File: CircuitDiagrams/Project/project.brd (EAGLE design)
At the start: 100 x 70 mm, 55 parts, among them IC1 UC3C, IC2 PCA9542A, IC3 MT48LC4M16A2TSOP54, IC4 TB6593FNGSSOP20, IC5 TB6593FNGSSOP20, J2 1BY2THROUGHHOLE, J3 1BY2THROUGHHOLE, Q1 OV7670, Q2 OV7670, Q3 VREGSOT-223, Q4 TCRT1010TH, Q5 TCRT1010TH, X2 MICROSDSMD

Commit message: Done some more on PCB, mainly adding decoupling capacitors (lots of)
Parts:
- added C10, C8: 4.7u, passives:C1206
- added C11, C13, C15, C17, C20: 33n, passives:C1206
- added C12, C14, C16, C19, C21, C7: 100n, passives:C1206
- added C18, C24, C27, C29, C32, C33, C42: 100n, passives:C0603
- added C22, C25, C28, C30, C43, C9: 33n, passives:C0603
- added C23, C26: 4.7u, passives:C0603
- added C34, C36, C38, C39: 0.1u, passives:C0603
- added C35, C37, C40, C41: 10u, passives:SMC_Z
- added C5: 2.2u, passives:C1206
- added C6: 1n, passives:C1206
- added Q6: CSM-7X-DU, crystal:CSM-7X-DU
- added R36: 1k5, passives:R0603
- moved C1 39.8 mm to (55.7, 31.4)
- moved C2 19.4 mm to (56.7, 51.8)
- moved S1 12.2 mm to (47.5, 50.3)
- moved R1 10.4 mm to (46.9, 55.1)
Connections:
- new net ADCREFN: C21.2, C22.2, IC1.35
- new net ADCREFP: C21.1, C22.1, IC1.34
- new net N$32: R36.1, X2.CD
- net +3V3: now also C10.1, C11.1, C12.1, C13.1, C14.1, C15.1, C16.1, C17.1, C18.1, C19.1, C20.1, C23.1, C24.1, C25.1, C26.1, C27.1, C28.1, C29.1, C30.1, C32.1, C33.1, C34.1, C35.+, C36.1, C37.+, C38.1, C39.1, C40.+, C41.+, C42.1, C43.1, C5.1, C6.1, C7.1, C8.1, C9.1
- net GND: now also C1.2, C10.2, C11.2, C12.2, C13.2, C14.2, C15.2, C16.2, C17.2, C18.2, C19.2, C2.2, C20.2, C23.2, C24.2, C25.2, C26.2, C27.2, C28.2, C29.2, C30.2, C32.2, C33.2, C34.2, C35.-, C36.2, C37.-, C38.2, C39.2, C40.-, C41.-, C42.2, C43.2, C5.2, C6.2, C7.2, C8.2, C9.2, X2.SW
- net PB0: now also C2.1, Q6.1
- net PB1: now also C1.1, Q6.2

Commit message: Placed all components. Need to confirm the circuit diagram and complete that before routing
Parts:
- C1, C10, C11, C12, C13, C14, C15, C16, C17, C19, C2, C20, C21, C5, C6, C7, C8: device passives:C1206 -> passives:C0603
- C3, C4: device passives:SMC_E -> passives:SMC_P
- moved R36 335.6 mm to (18.0, 62.0), turned to 270 degrees
- moved C43 333.4 mm to (98.0, 30.0), turned to 90 degrees
- moved C42 322.6 mm to (94.0, 30.0), turned to 90 degrees
- moved C35 296.5 mm to (16.0, 45.0), flipped to the bottom
- moved C38 296.5 mm to (15.0, 29.0), flipped to the bottom
- moved C37 294.6 mm to (16.0, 39.0), flipped to the bottom
- moved C39 293.2 mm to (15.0, 26.0), flipped to the bottom
- moved C36 289.6 mm to (16.0, 42.0), flipped to the bottom
- moved C34 287.6 mm to (16.0, 48.0), flipped to the bottom
- moved C40 284.5 mm to (15.0, 23.0), flipped to the bottom
- moved C41 281.3 mm to (15.0, 20.0), flipped to the bottom
- moved C32 281.0 mm to (3.00, 51.0), turned to 180 degrees
- moved C30 278.6 mm to (98.0, 39.0), turned to 90 degrees
- moved C29 273.4 mm to (94.0, 39.0), turned to 90 degrees
- moved C33 266.6 mm to (79.0, 20.0), flipped to the bottom, turned to 270 degrees
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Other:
- outline, holes or cut-outs redrawn

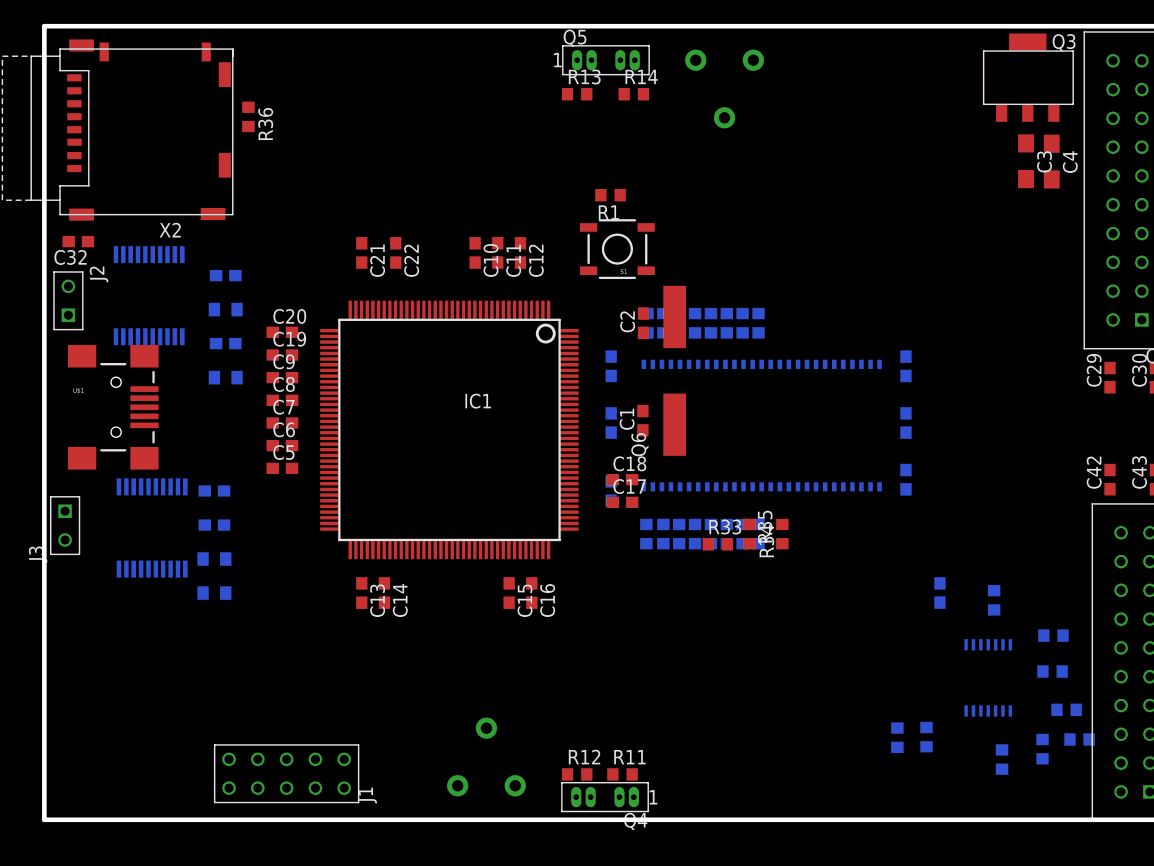
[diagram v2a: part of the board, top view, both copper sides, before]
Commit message: Wired up GPIOs to Devices. Need to add a UI.
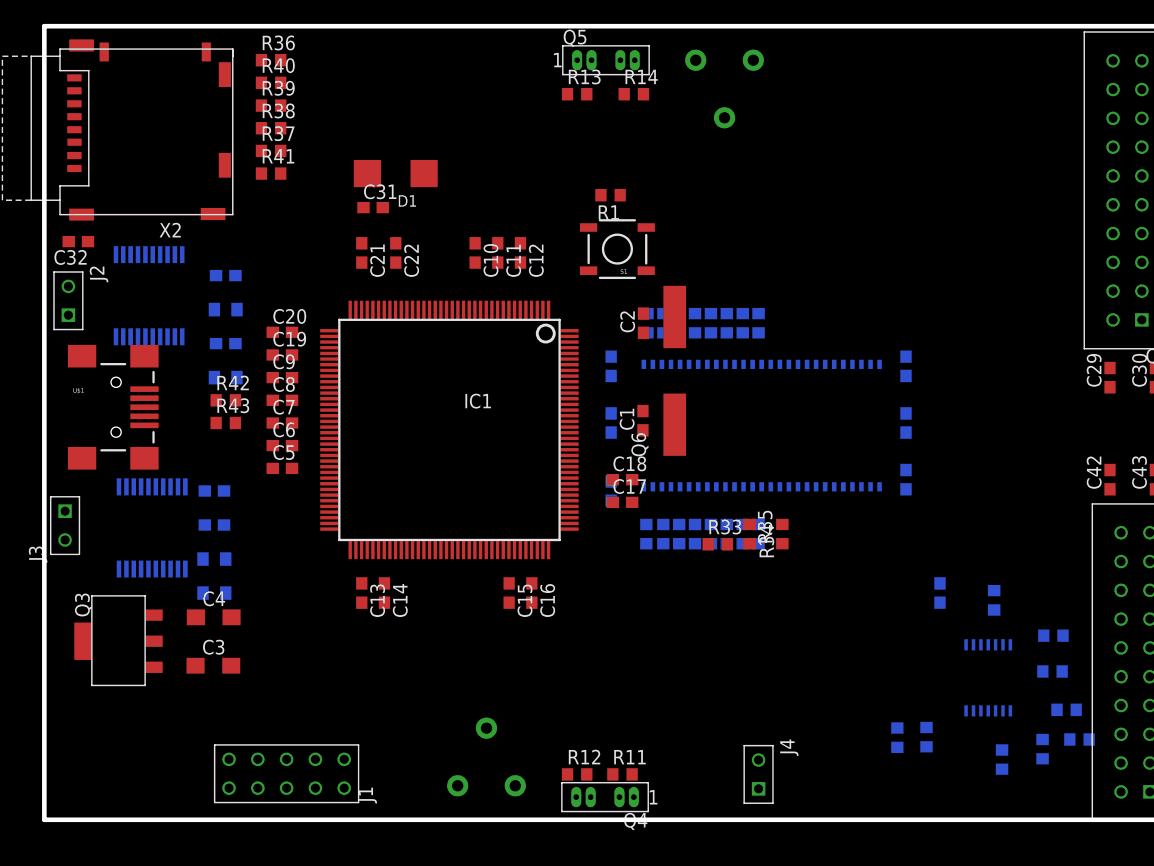
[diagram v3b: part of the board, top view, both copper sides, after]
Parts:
- added C31: 100n, passives:C0603
- added D1: DIODESMD, Semiconductors:SMC_C
- added J4: 1BY2THROUGHHOLE, Headers:1BY2
- added R37, R38, R39, R40: 68R, passives:R0603
- added R41: 100k, passives:R0603
- added R42, R43: 39R, passives:R0603
- R36: value 1k5 -> 100k
- moved Q3 94.2 mm to (6.69, 15.8), turned to 90 degrees
- moved C3 84.4 mm to (14.9, 13.6), turned to 0 degrees
- moved C4 84.1 mm to (14.9, 17.9), turned to 0 degrees
- moved R36 5.39 mm to (20.0, 67.0), turned to 0 degrees
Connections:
- removed net MOTOR_REF_1: R15.1
- removed net MOTOR_REF_2: R16.1
- removed net MOTOR_SENSE_1: Q4.COLLECTOR, R12.1
- removed net MOTOR_SENSE_2: Q5.COLLECTOR, R14.1
- removed net N$32: R36.1, X2.CD
- removed net OV_NOE0: Q1.NOE
- removed net OV_NOE1: Q2.NOE
- removed net OV_RCLK0: Q1.RCLK
- removed net OV_RCLK1: Q2.RCLK
- removed net OV_RRST0: Q1.RRST
- removed net OV_RRST1: Q2.RRST
- removed net OV_VSYNC0: Q1.VSYNC
- removed net OV_VSYNC1: Q2.VSYNC
- removed net OV_WEN0: Q1.WEN
- removed net OV_WEN1: Q2.WEN
- removed net OV_WRST0: Q1.WRST
- removed net OV_WRST1: Q2.WRST
- new net N$23: R37.2, R41.2, X2.1
- new net N$25: R38.2, X2.2
- new net N$26: R39.2, X2.5
- new net N$27: R40.2, X2.7
- new net N$28: IC1.50, R42.2
- new net N$29: IC1.51, R43.2
- net +3V3: now also D1.+, R41.1, X2.SW
- net DM: now also R42.1; no longer IC1.50
- net DP: now also R43.1; no longer IC1.51
- net GND: now also C31.2, R36.2; no longer X2.SW
- net PA15: now also Q1.RRST
- net PA16: now also C31.1, D1.-
- net PA19: now also Q1.RCLK
- net PA20: now also Q1.WEN
- net PA21: now also Q1.WRST
- net PA22: now also Q2.RRST
- net PA23: now also Q2.RCLK
- net PA24: now also Q2.WEN
- net PA25: now also Q2.WRST
- net PA26: now also Q2.VSYNC
- net PA27: now also Q2.NOE
- net PA28: now also Q1.NOE
- net PA29: now also Q1.VSYNC
- net PA4: now also U$1.ID
- net PA6: now also Q4.COLLECTOR, R12.1
- net PA7: now also R15.1
- net PA8: now also Q5.COLLECTOR, R14.1
- net PA9: now also R16.1
- net PB10: now also IC4.19; no longer X2.2
- net PB11: now also IC4.2; no longer X2.7
- net PB12: no longer X2.5
- net PB13: now also IC5.2; no longer X2.1
- net PB14: now also IC5.19
- net PB15: now also IC5.18
- net PB16: now also IC5.3
- net PB19: now also R38.1
- net PB20: now also R40.1
- net PB21: now also R39.1
- net PB25: now also R37.1
- net PB26: now also R36.1, X2.CD
- net PB8: now also IC4.3
- net PB9: now also IC4.18
- net PC2: now also J4.1
- net PC3: now also J4.2
- net PD10: now also IC3.32
- net PD11: now also IC3.33
- net PD12: now also IC3.34
- net PD14: now also IC3.22
- net PD15: now also IC3.35
- net PD16: now also IC3.21
- net PD17: now also IC3.20
- net PD3: now also IC3.23
- net PD4: now also IC3.24
- net PD5: now also IC3.25
- net PD6: now also IC3.26
- net PD7: now also IC3.29
- net PD8: now also IC3.30
- net PD9: now also IC3.31

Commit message: Changed JTAG Connection to include the Reset Pin.
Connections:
- net RESET_N: now also J1.6
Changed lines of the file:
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@@
 <signals>
 <signal name="GND">
-<contactref element="J1" pad="2"/>
-<contactref element="J1" pad="10"/>
 <contactref element="IC1" pad="6"/>
 <contactref element="IC1" pad="37"/>
@@
 <contactref element="R36" pad="2"/>
 <contactref element="C31" pad="2"/>
-<wire x1="16.515" y1="17.86" x2="94.27" y2="56.79" width="0" layer="19" extent="1-1"/>
-<wire x1="16.485" y1="13.59" x2="16.515" y2="17.86" width="0" layer="19" extent="1-1"/>
-<wire x1="9.69" y1="13.45" x2="16.485" y2="13.59" width="0" layer="19" extent="1-1"/>
+<contactref element="J1" pad="10"/>
+<contactref element="J1" pad="2"/>
 <wire x1="94.27" y1="44.09" x2="94.27" y2="56.79" width="0" layer="19" extent="1-1"/>
 <wire x1="94" y1="39.85" x2="94.27" y2="44.09" width="0" layer="19" extent="1-1"/>
@@
 <wire x1="11.135" y1="22.115" x2="11.785" y2="22.115" width="0" layer="19" extent="16-16"/>
 <wire x1="14" y1="20" x2="12.435" y2="22.115" width="0" layer="19" extent="16-16"/>
+<wire x1="16.515" y1="17.86" x2="14" y2="20" width="0" layer="19" extent="1-16"/>
+<wire x1="16.485" y1="13.59" x2="16.515" y2="17.86" width="0" layer="19" extent="1-1"/>
+<wire x1="9.69" y1="13.45" x2="16.485" y2="13.59" width="0" layer="19" extent="1-1"/>
+<wire x1="16.29" y1="2.79" x2="16.485" y2="13.59" width="0" layer="19" extent="1-1"/>
+<wire x1="26.45" y1="2.79" x2="16.29" y2="2.79" width="0" layer="19" extent="1-1"/>
 <wire x1="2.65" y1="63.159" x2="2.15" y2="51" width="0" layer="19" extent="1-1"/>
 <wire x1="94.98" y1="2.46" x2="94.98" y2="15.16" width="0" layer="19" extent="1-1"/>
-<wire x1="20.85" y1="67" x2="29.85" y2="54" width="0" layer="19" extent="1-1"/>
-<wire x1="41.54" y1="3" x2="41" y2="19.15" width="0" layer="19" extent="1-1"/>
+<wire x1="41.54" y1="3" x2="26.45" y2="2.79" width="0" layer="19" extent="1-1"/>
 <wire x1="48.19" y1="2" x2="41.54" y2="3" width="0" layer="19" extent="1-1"/>
 <wire x1="50.73" y1="2" x2="48.19" y2="2" width="0" layer="19" extent="1-1"/>
-<wire x1="26.45" y1="2.79" x2="41.54" y2="3" width="0" layer="19" extent="1-1"/>
-<wire x1="16.29" y1="2.79" x2="26.45" y2="2.79" width="0" layer="19" extent="1-1"/>
+<wire x1="20.85" y1="67" x2="29.85" y2="54" width="0" layer="19" extent="1-1"/>
 <wire x1="48.27" y1="67" x2="48.01" y2="48.435" width="0" layer="19" extent="1-1"/>
 <wire x1="50.81" y1="67" x2="48.27" y2="67" width="0" layer="19" extent="1-1"/>
@@
 <contactref element="S1" pad="4"/>
 <contactref element="S1" pad="3"/>
+<contactref element="J1" pad="6"/>
 <wire x1="53.09" y1="52.245" x2="50.795" y2="55.09" width="0" layer="19" extent="1-1"/>
 <wire x1="48.01" y1="52.245" x2="50.795" y2="55.09" width="0" layer="19" extent="1-1"/>
 <wire x1="46.33" y1="42.14" x2="48.01" y2="52.245" width="0" layer="19" extent="1-1"/>
+<wire x1="21.37" y1="2.79" x2="46.33" y2="42.14" width="0" layer="19" extent="1-1"/>
 </signal>
 <signal name="INT">

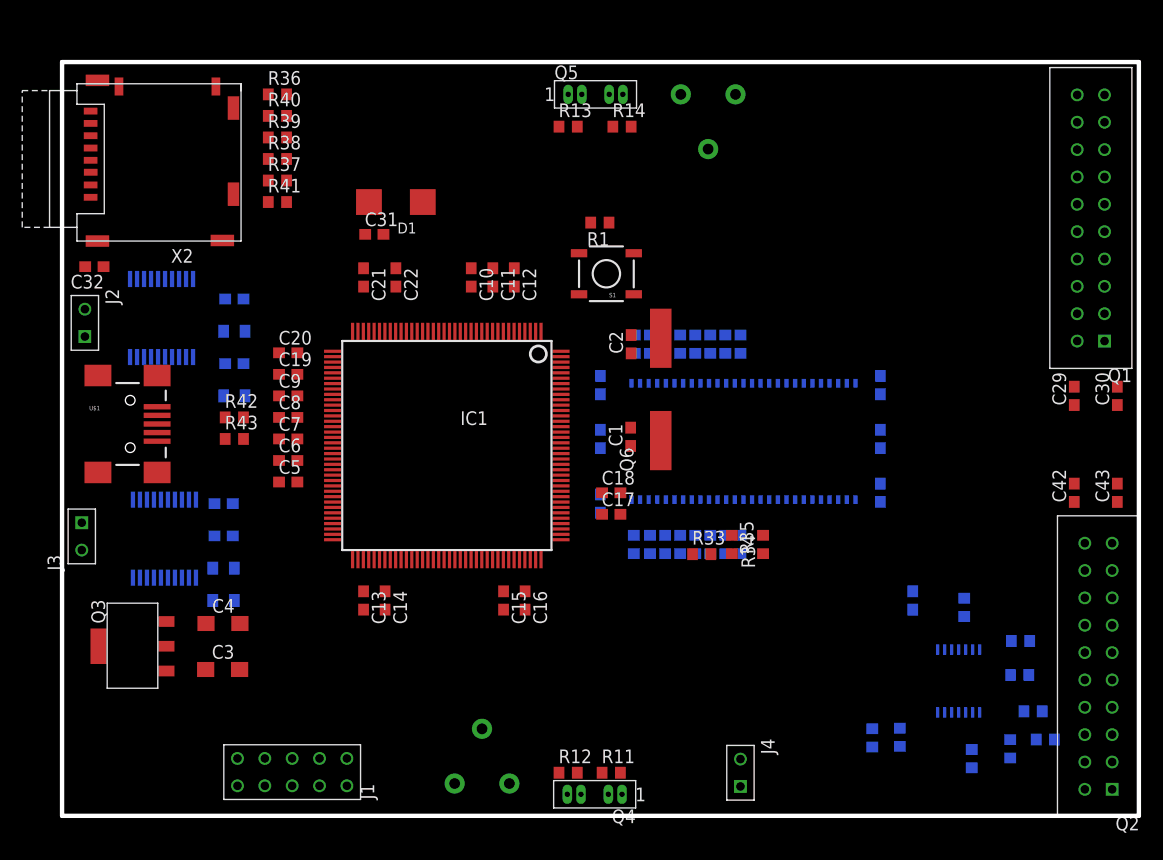
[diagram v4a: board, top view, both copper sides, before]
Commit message: Added LEDs to the deisgn and a USART Port.
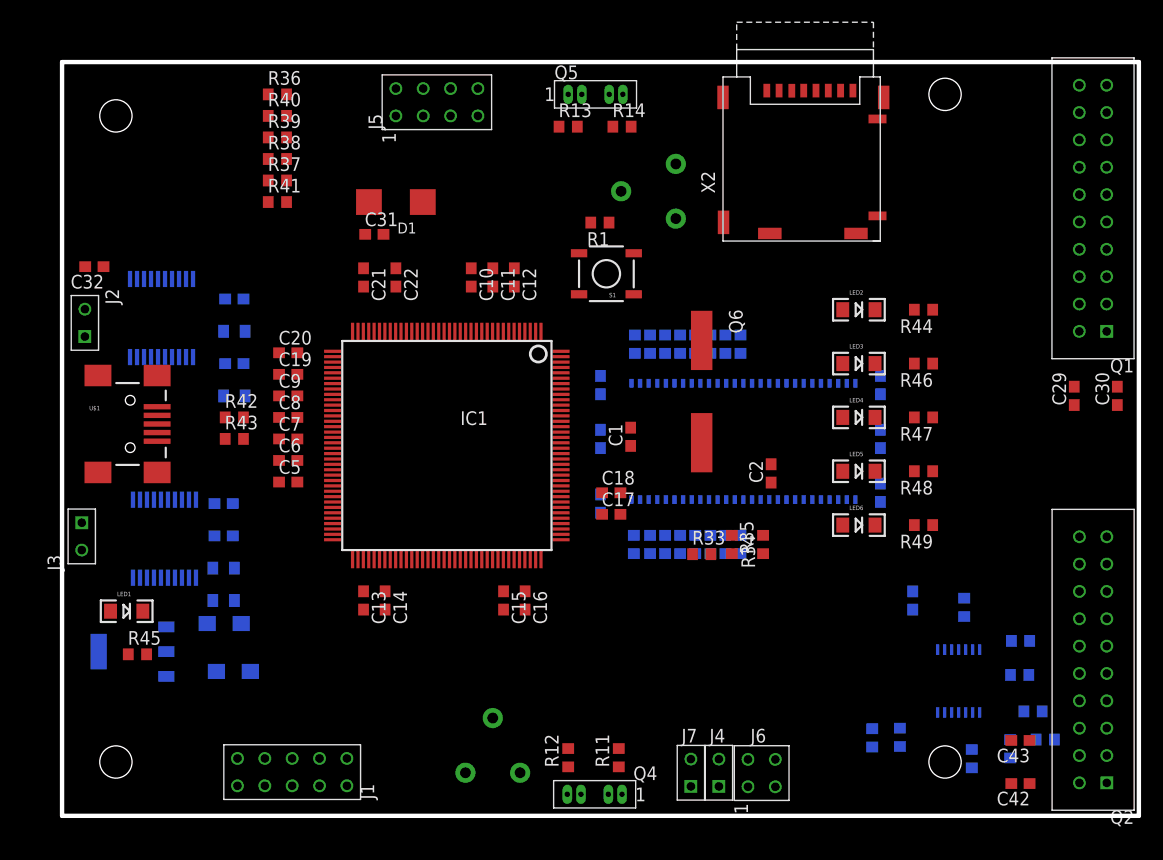
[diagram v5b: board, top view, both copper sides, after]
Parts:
- added J5: 8PIN1.27MM2X4TH, Headers:1.27MM2X4TH
- added J6: 4PIN1.27MM2X2TH, Headers:1.27MM2X2TH
- added J7: 1BY2THROUGHHOLE, Headers:1BY2
- added LED1, LED2, LED3, LED4, LED5, LED6: (no value), Semiconductors:LED-1206
- added R44, R45, R46, R47, R48, R49: 330R, passives:R0603
- moved X2 60.0 mm to (69.0, 61.0), turned to 0 degrees
- moved C42 27.5 mm to (89.0, 3.00), turned to 180 degrees
- moved C43 24.7 mm to (89.0, 7.00), turned to 180 degrees
- moved C2 17.7 mm to (65.8, 31.8)
- moved R16 9.49 mm to (57.0, 58.0), turned to 180 degrees
- moved Q6 3.81 mm to (59.4, 39.4), turned to 270 degrees
- moved J4 2.00 mm to (61.0, 4.00)
- moved R11 1.57 mm to (51.7, 5.40), turned to 90 degrees
- moved R15 1.41 mm to (40.0, 4.00)
- moved R12 1.40 mm to (47.0, 5.40), turned to 90 degrees
- moved C3 1.02 mm to (15.9, 13.4), flipped to the bottom, turned to 180 degrees
- moved Q1 0.92 mm to (97.0, 45.0)
- moved Q2 0.78 mm to (97.0, 3.06)
- moved Q3 0.50 mm to (6.69, 15.2), flipped to the bottom, turned to 270 degrees
- moved C4 0.12 mm to (15.1, 17.9), flipped to the bottom
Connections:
- new net N$30: LED2.C, R44.2
- new net N$31: LED1.C, R45.2
- new net N$32: LED3.C, R46.2
- new net N$33: LED4.C, R47.2
- new net N$34: LED5.C, R48.2
- new net N$35: LED6.C, R49.2
- net +3V3: now also J6.1
- net +5V: now also J6.4
- net GND: now also J6.2, J6.3, R44.1, R45.1, R46.1, R47.1, R48.1, R49.1
- net PB12: now also LED1.A
- net PB17: now also LED2.A
- net PB18: now also LED3.A
- net PB19: now also J5.1
- net PB20: now also J5.2
- net PB21: now also J5.3
- net PB22: now also J5.5
- net PB23: now also J5.6
- net PB24: now also J5.7
- net PB25: now also J5.8
- net PB27: now also LED4.A
- net PB28: now also LED5.A
- net PB29: now also LED6.A
- net PC18: now also IC3.22
- net PC4: now also J7.1
- net PC5: now also J7.2
- net PD10: now also IC3.30; no longer IC3.32
- net PD11: now also IC3.31; no longer IC3.33
- net PD12: now also IC3.32; no longer IC3.34
- net PD14: now also IC3.33; no longer IC3.22
- net PD15: now also IC3.34; no longer IC3.35
- net PD16: no longer IC3.21
- net PD17: now also IC3.35; no longer IC3.20
- net PD20: now also IC3.20
- net PD21: now also IC3.21
- net PD24: now also IC3.39
- net PD3: now also IC3.15; no longer IC3.23
- net PD4: no longer IC3.24
- net PD5: now also IC3.23; no longer IC3.25
- net PD6: now also IC3.24; no longer IC3.26
- net PD7: now also IC3.25; no longer IC3.29
- net PD8: now also IC3.26; no longer IC3.30
- net PD9: now also IC3.29; no longer IC3.31

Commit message: Completed First Draft of Schematic
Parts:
- added J8: 10PIN1.27MM2X5TH, Headers:1.27MM2X5TH
- added LED7: (no value), Semiconductors:LED-1206
- added R50: 330R, passives:R0603
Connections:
- removed net OVDATA0: Q1.D0, Q2.D0
- removed net OVDATA1: Q1.D1, Q2.D1
- removed net OVDATA2: Q1.D2, Q2.D2
- removed net OVDATA3: Q1.D3, Q2.D3
- removed net OVDATA4: Q1.D4, Q2.D4
- removed net OVDATA5: Q1.D5, Q2.D5
- removed net OVDATA6: Q1.D6, Q2.D6
- removed net OVDATA7: Q1.D7, Q2.D7
- removed net PA11: IC1.28
- new net N$36: LED7.C, R50.2
- net +3V3: now also LED7.A; no longer C5.1, C6.1
- net GND: now also R50.1
- net PA10: now also J8.2
- net PA12: now also J8.3
- net PA13: now also J8.4
- net PA14: now also J8.5
- net PA16: now also IC1.28
- net PA5: now also J8.1
- net PB0: now also Q1.D0, Q2.D0; no longer C2.1, Q6.1
- net PB1: now also Q1.D1, Q2.D1; no longer C1.1, Q6.2
- net PB2: now also Q1.D2, Q2.D2
- net PB3: now also Q1.D3, Q2.D3
- net PB30: now also C2.1, Q6.1
- net PB31: now also C1.1, Q6.2
- net PB4: now also Q1.D4, Q2.D4
- net PB5: now also Q1.D5, Q2.D5
- net PB6: now also Q1.D6, Q2.D6
- net PB7: now also Q1.D7, Q2.D7
- net PC0: now also J8.10
- net PC1: now also J8.9
- net PC13: now also J8.7
- net PC6: now also J8.8
- net PD29: now also J8.6
- net VDDCORE: now also C5.1, C6.1
